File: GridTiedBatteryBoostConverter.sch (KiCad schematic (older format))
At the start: 55 parts, among them J101 Battery Connection, J103 Solar Panels, Q101 IXFP36N20X3, Q102 BC847B-13-F, Q103 SSM3K329R, Q104 SSM3J334R, U101 OPA2837DGK, U102 UCC2800DTR

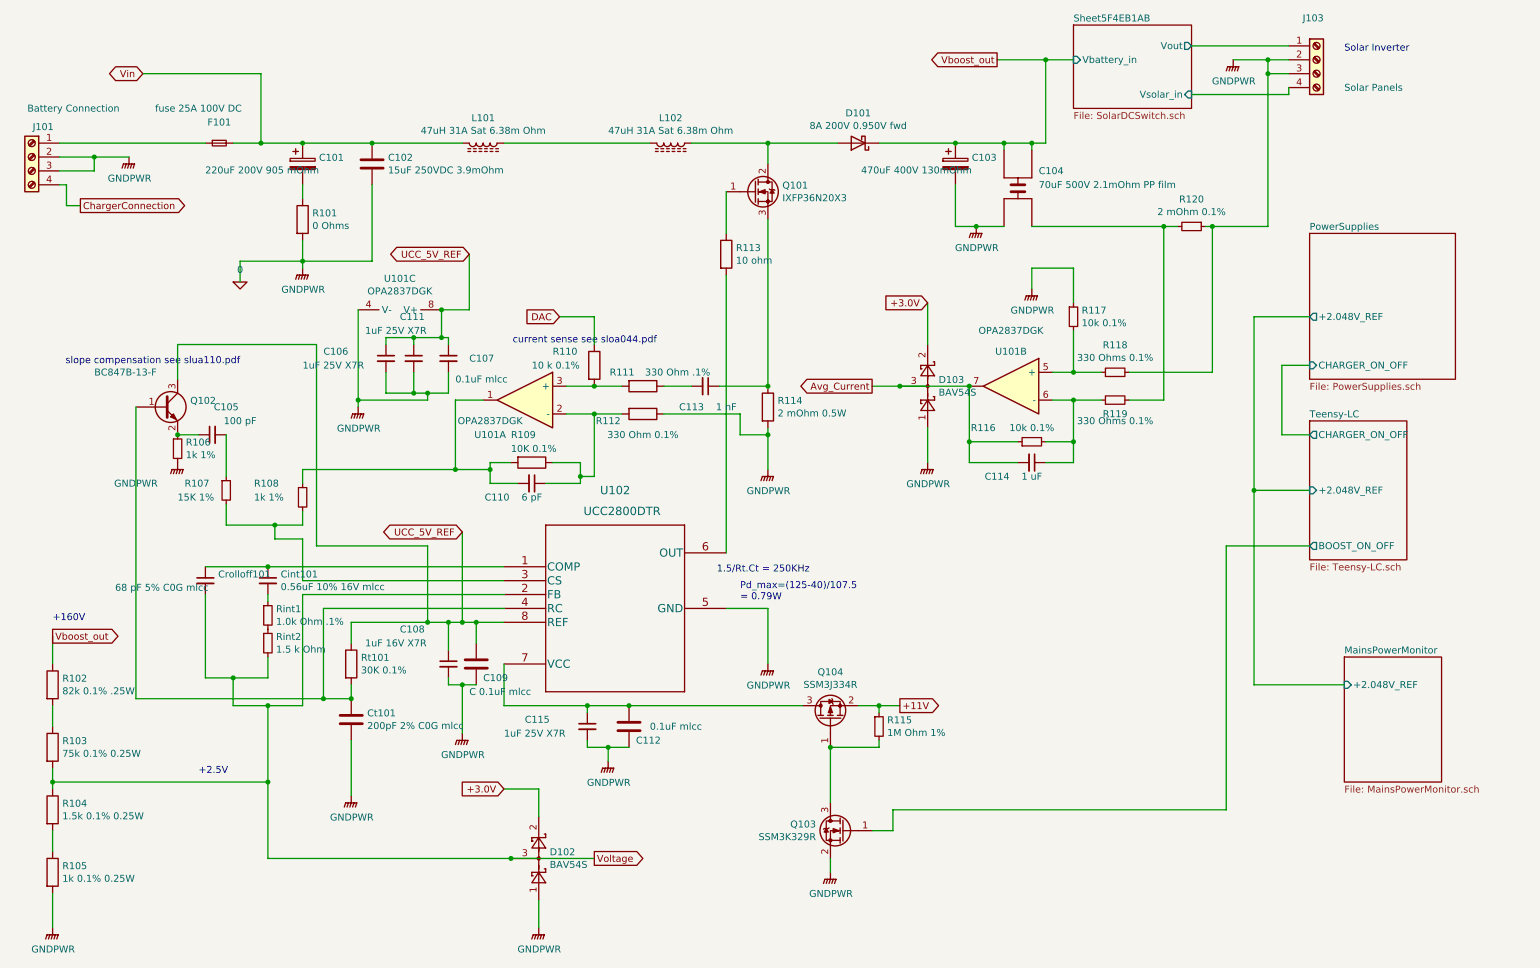
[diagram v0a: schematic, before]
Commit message: started routing backing up tonnes of changes,2.048V reference changed to 2.5V ref, to match ucc2800, cos to change to a version with a 2V feedback, would require me to update the Oscillator cap and resistor,and also recalulate the class 2 loop compensation components etc.  Move the location of the teensy LC and added the ESP-WROOM-o2 wifi module.
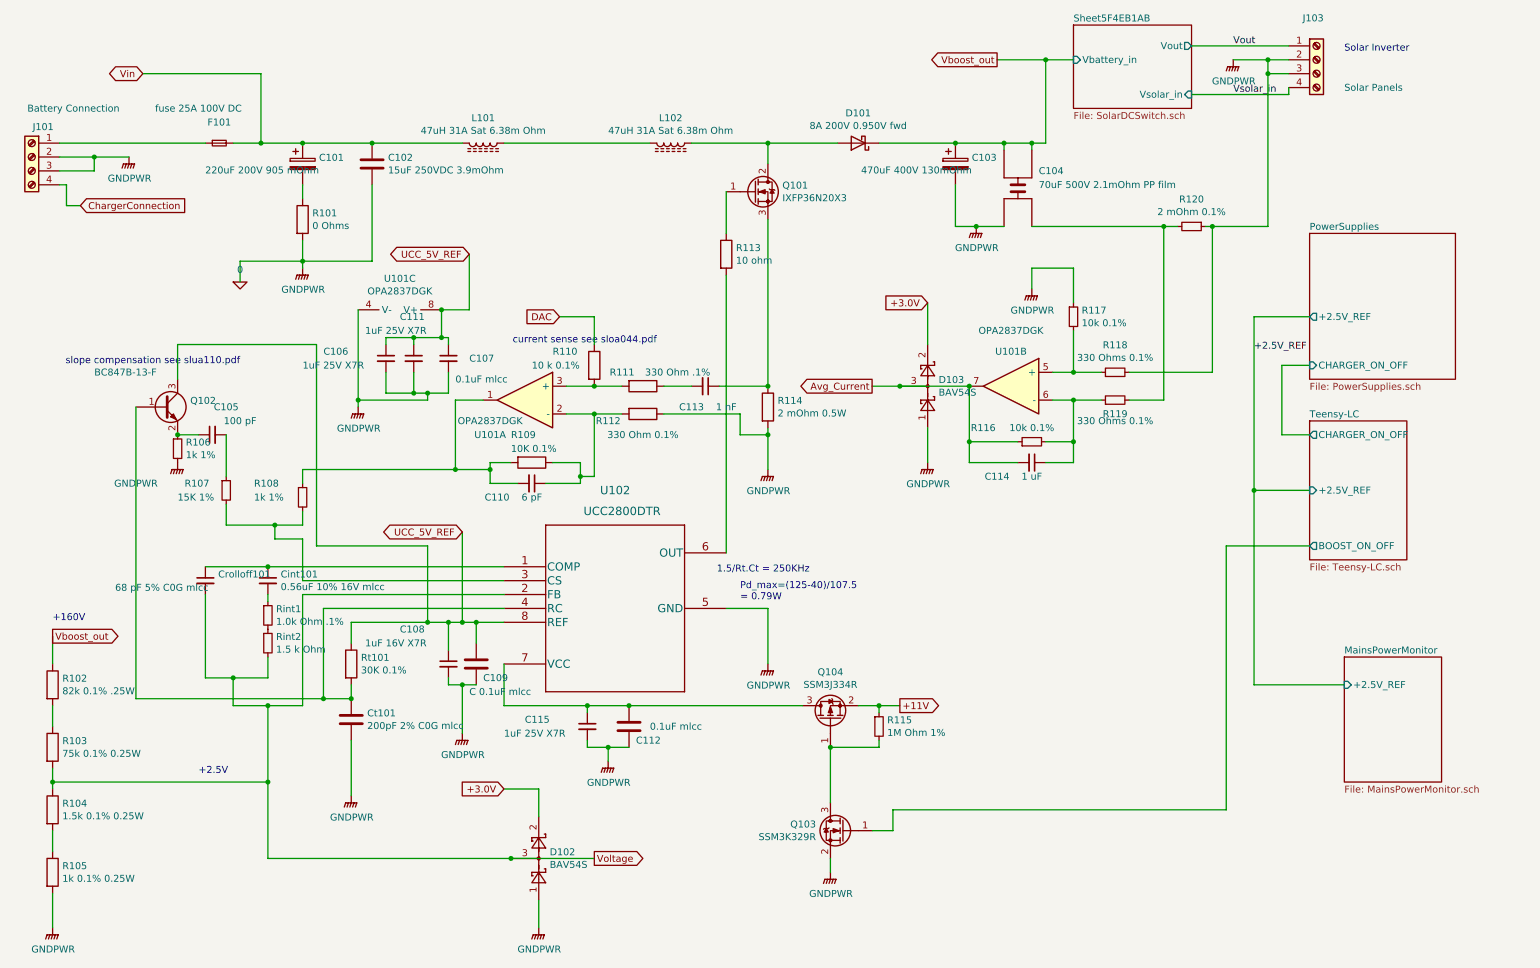
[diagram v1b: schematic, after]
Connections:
- net Sheet5F4EB1AB/Vout renamed Vout
- net Sheet5F4EB1AB/Vsolar_in renamed Vsolar_in
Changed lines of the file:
@@
 F2 "CHARGER_ON_OFF" O L 9850 3800 50
 F3 "BOOST_ON_OFF" O L 9850 4600 50
-F4 "+2.048V_REF" I L 9850 4200 50
+F4 "+2.5V_REF" I L 9850 4200 50
 $EndSheet
 Text GLabel 6700 3450 0    50   Output ~ 0
@@
 F1 "PowerSupplies.sch" 50
 F2 "CHARGER_ON_OFF" I L 9850 3300 50
-F3 "+2.048V_REF" O L 9850 2950 50
+F3 "+2.5V_REF" O L 9850 2950 50
 $EndSheet
 $Comp
@@
 F0 "MainsPowerMonitor" 50
 F1 "MainsPowerMonitor.sch" 50
-F2 "+2.048V_REF" I L 10100 5600 50
+F2 "+2.5V_REF" I L 10100 5600 50
 $EndSheet
 $Comp
@@
 Wire Wire Line
 	4650 5750 4950 5750
-Text GLabel 1000 2150 2    50   Output ~ 0
+Text GLabel 1000 2150 2    50   Input ~ 0
 ChargerConnection
 $Comp
@@
 Wire Wire Line
 	3650 3100 3650 3150
+Text Label 9300 1350 0    50   ~ 0
+Vsolar_in
+Text Label 9300 1000 0    50   ~ 0
+Vout
+Text Label 9450 3200 0    50   ~ 0
++2.5V_REF
 $EndSCHEMATC

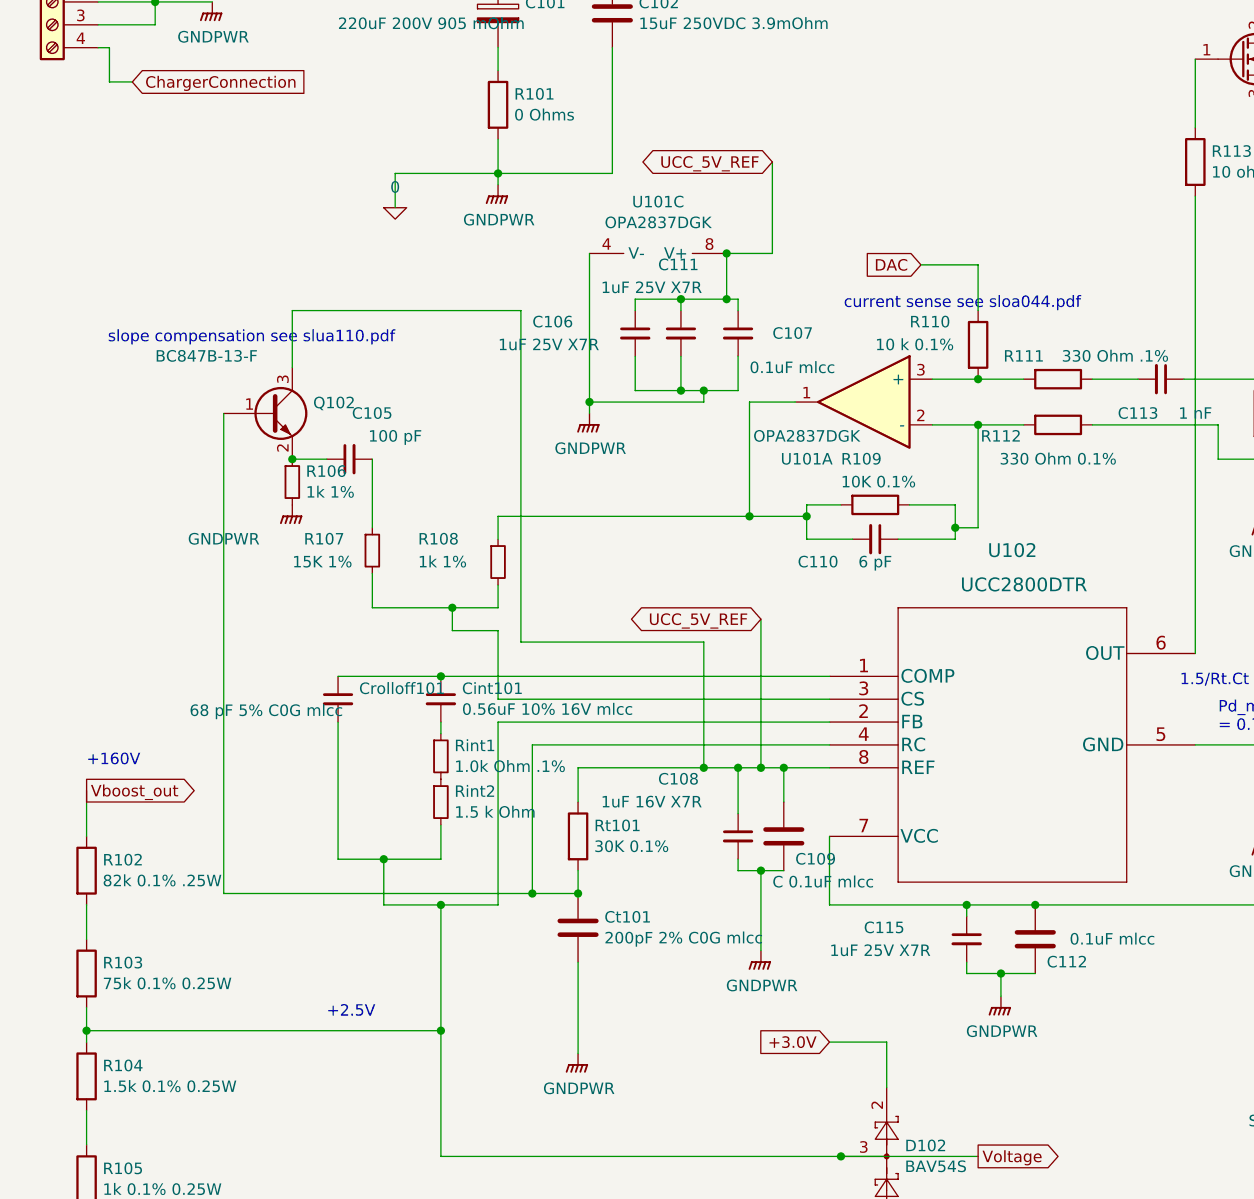
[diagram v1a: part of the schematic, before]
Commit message: added testpoints
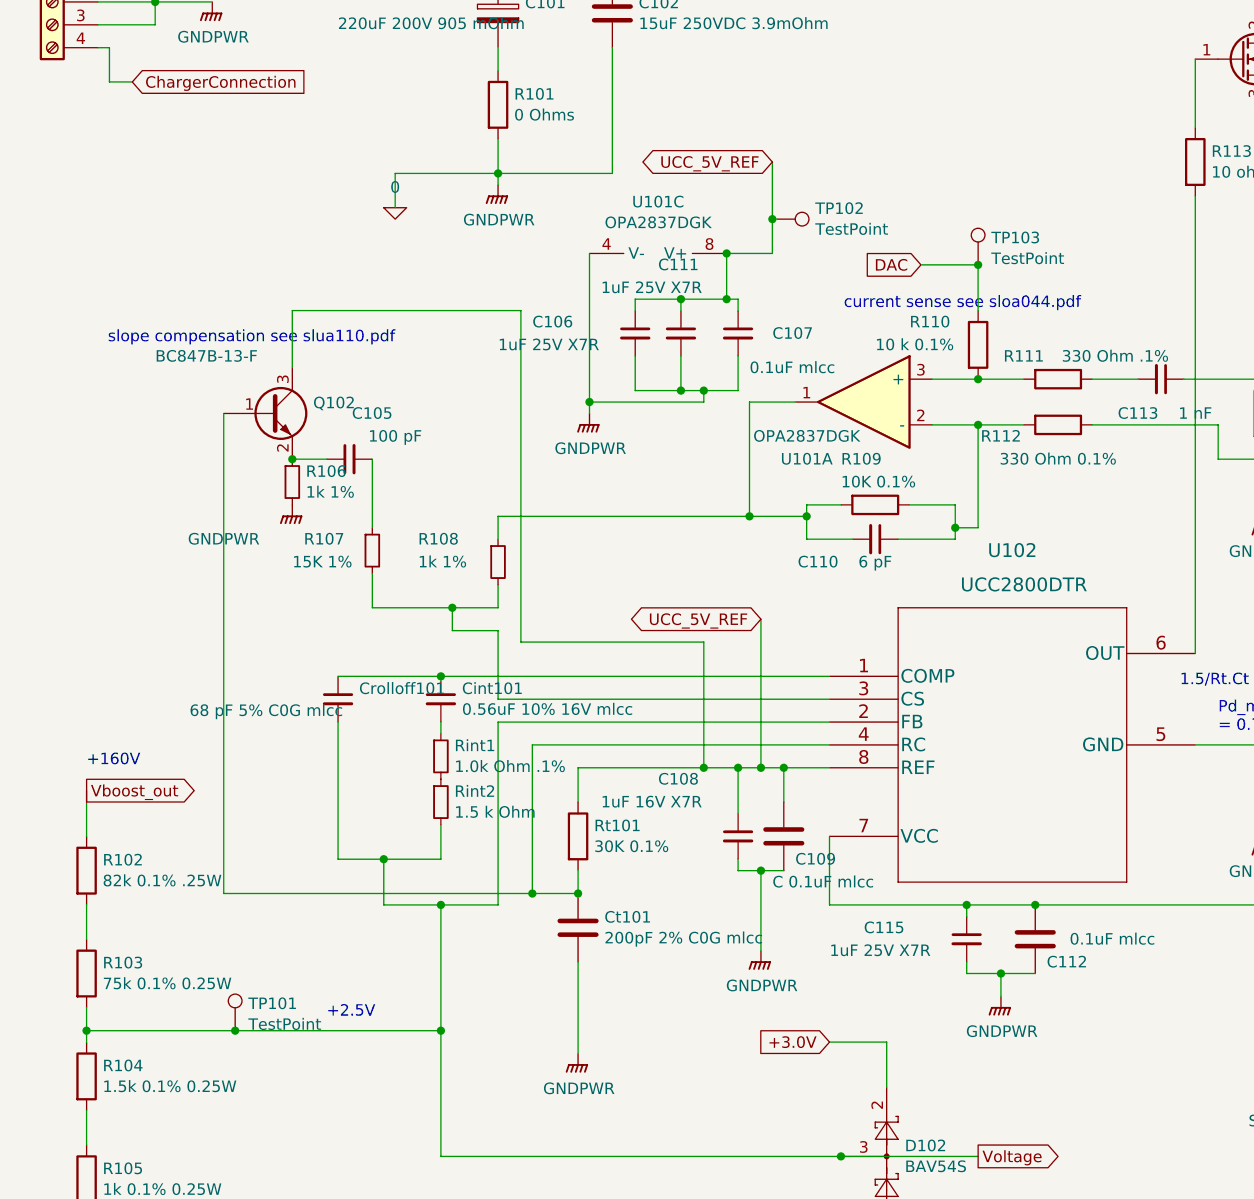
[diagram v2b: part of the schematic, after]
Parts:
- added TP101, TP102, TP103: TestPoint, Measurement_Points:Measurement_Point_Square-SMD-Pad_Big, symbol Connector:TestPoint
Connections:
- net DAC: now also TP103.1
- net UCC_5V_REF: now also TP102.1
- net Voltage: now also TP101.1
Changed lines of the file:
@@
 	3950 4050 3950 4000
 Wire Wire Line
-	800  6300 2350 6300
+	800  6300 1450 6300
 $Comp
 L Device:R_Small R120
@@
 UCC_5V_REF
 Wire Wire Line
-	3800 2900 3800 2500
+	3800 2900 3800 2750
 Wire Wire Line
 	3600 2900 3800 2900
@@
 Text Label 9450 3200 0    50   ~ 0
 +2.5V_REF
+$Comp
+L Connector:TestPoint TP?
+U 1 1 6050D700
+P 1450 6300
+AR Path="/5EBD6442/6050D700" Ref="TP?"  Part="1"
+AR Path="/5EF73D52/6050D700" Ref="TP?"  Part="1"
+AR Path="/6050D700" Ref="TP101"  Part="1"
+F 0 "TP101" H 1508 6418 50  0000 L CNN
+F 1 "TestPoint" H 1508 6327 50  0000 L CNN
+F 2 "Measurement_Points:Measurement_Point_Square-SMD-Pad_Big" H 1650 6300 50  0001 C CNN
+F 3 "~" H 1650 6300 50  0001 C CNN
+	1    1450 6300
+	1    0    0    -1
+$EndComp
+$Comp
+L Connector:TestPoint TP?
+U 1 1 60519D43
+P 3800 2750
+AR Path="/5EBD6442/60519D43" Ref="TP?"  Part="1"
+AR Path="/5EF73D52/60519D43" Ref="TP?"  Part="1"
+AR Path="/60519D43" Ref="TP102"  Part="1"
+F 0 "TP102" V 3754 2938 50  0000 L CNN
+F 1 "TestPoint" V 3845 2938 50  0000 L CNN
+F 2 "Measurement_Points:Measurement_Point_Square-SMD-Pad_Big" H 4000 2750 50  0001 C CNN
+F 3 "~" H 4000 2750 50  0001 C CNN
+	1    3800 2750
+	0    1    1    0
+$EndComp
+Connection ~ 3800 2750
+Wire Wire Line
+	3800 2750 3800 2500
+$Comp
+L Connector:TestPoint TP?
+U 1 1 6051C0A5
+P 4700 2950
+AR Path="/5EBD6442/6051C0A5" Ref="TP?"  Part="1"
+AR Path="/5EF73D52/6051C0A5" Ref="TP?"  Part="1"
+AR Path="/6051C0A5" Ref="TP103"  Part="1"
+F 0 "TP103" H 4758 3068 50  0000 L CNN
+F 1 "TestPoint" H 4758 2977 50  0000 L CNN
+F 2 "Measurement_Points:Measurement_Point_Square-SMD-Pad_Big" H 4900 2950 50  0001 C CNN
+F 3 "~" H 4900 2950 50  0001 C CNN
+	1    4700 2950
+	1    0    0    -1
+$EndComp
+Connection ~ 4700 2950
+Connection ~ 1450 6300
+Wire Wire Line
+	1450 6300 2350 6300
 $EndSCHEMATC
